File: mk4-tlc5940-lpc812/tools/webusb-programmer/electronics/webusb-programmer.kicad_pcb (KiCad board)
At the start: 2 copper layers, 38 x 20 mm, 29 parts, among them J1 USB_B_Micro, J2 Light Controller, Q1 PMV30UN, U1 MCP1703A-3302_SOT23, U2 SAMD21E15A-MU, U3 STMPS2141STR

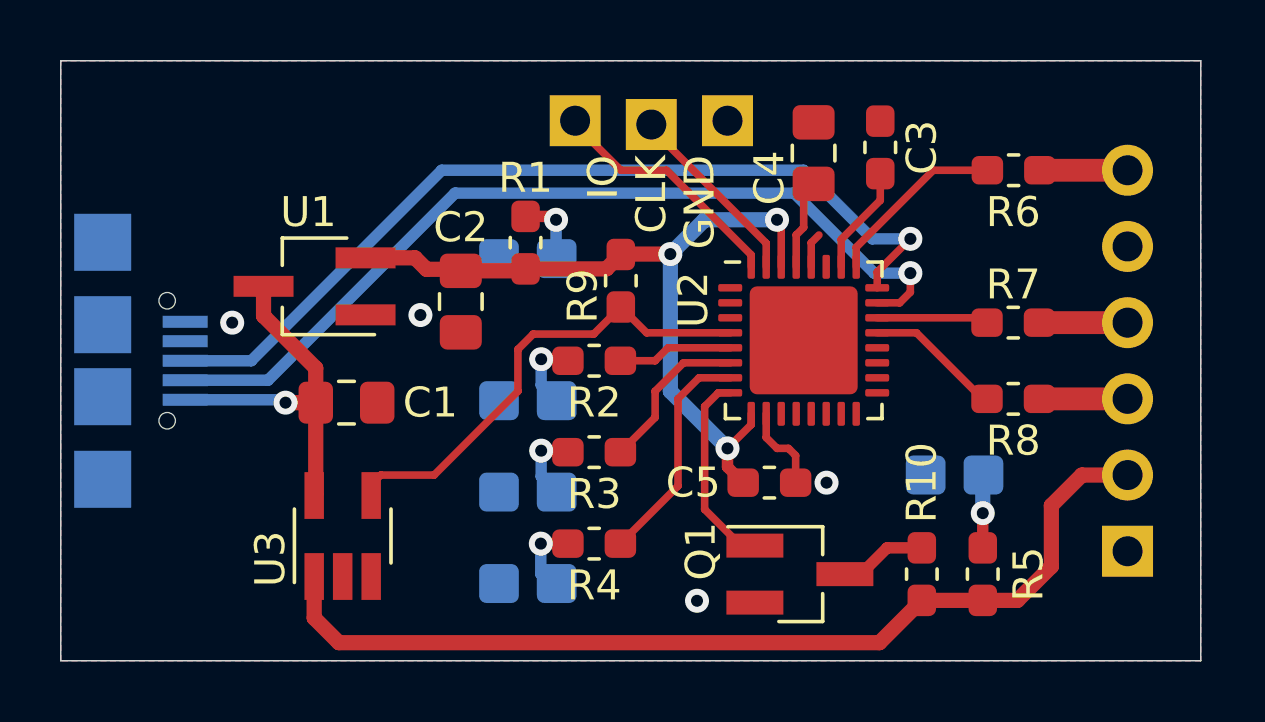
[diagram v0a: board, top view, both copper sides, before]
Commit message: Add CH3 IO and reannotate all components
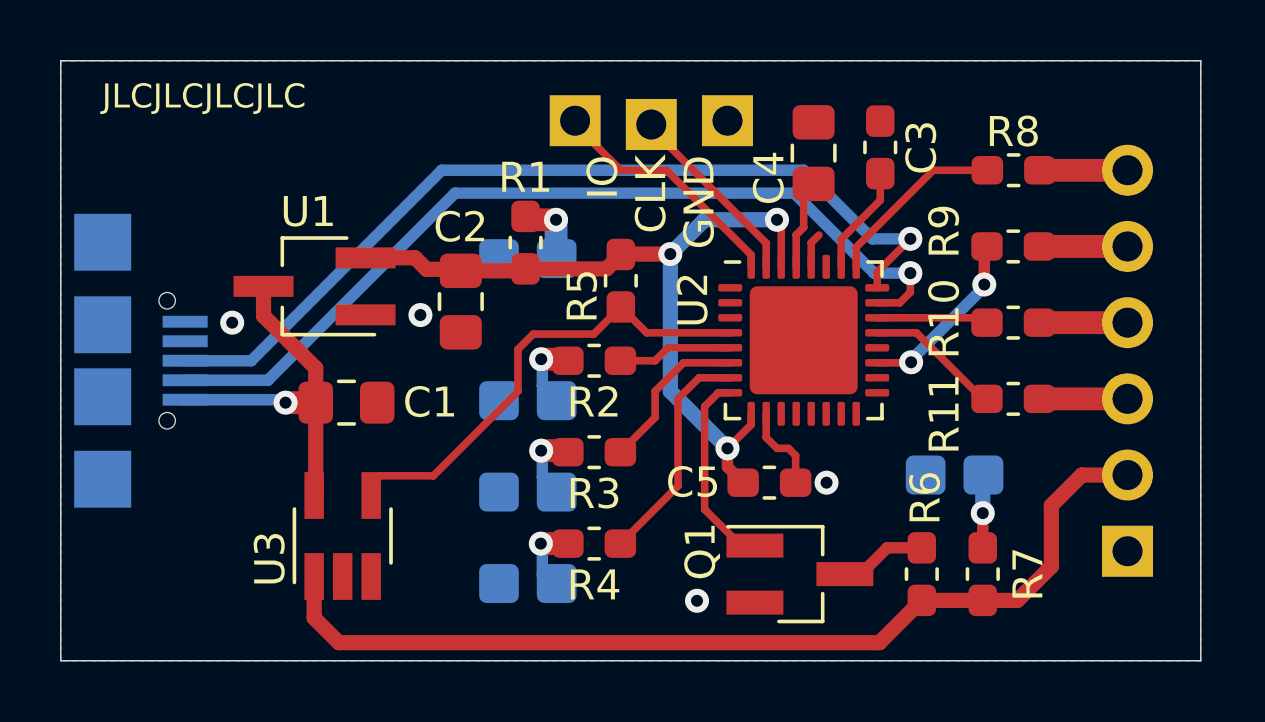
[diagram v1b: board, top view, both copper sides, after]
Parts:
- added R9: 1k, Resistor_SMD:R_0603_1608Metric_Pad1.05x0.95mm_HandSolder, F.Cu at (131.8, 96.2)
- renumbered R7 to R10, R8 to R11, R9 to R5, R10 to R6, R5 to R7, R6 to R8
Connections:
- U2 pad 19: Net-(U2-Pad19) -> /CH3
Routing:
- net /CH3: track 0.00 -> 6.05 mm, vias 0 -> 2
- net Net-(J2-Pad5): track 0.00 -> 2.94 mm
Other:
- board text added: "JLCJLCJLCJLC"

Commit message: Change LED resistor values after testing
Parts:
- R1, R7: value 1k2 -> 1k8
- R2: value 1k2 -> 2k7
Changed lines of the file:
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@@
       (effects (font (size 1 1) (thickness 0.15)))
     )
-    (fp_text value 1k2 (at 2.413 -0.127 90) (layer F.Fab)
+    (fp_text value 1k8 (at 2.413 -0.127 90) (layer F.Fab)
       (effects (font (size 1 1) (thickness 0.15)))
     )
@@
       (effects (font (size 1 1) (thickness 0.15)))
     )
-    (fp_text value 1k2 (at -2.413 0) (layer F.Fab)
+    (fp_text value 2k7 (at -2.413 0) (layer F.Fab)
       (effects (font (size 1 1) (thickness 0.15)))
     )
@@
       (effects (font (size 1 1) (thickness 0.15)))
     )
-    (fp_text value 1k2 (at 0.889 -1.143 90) (layer F.Fab)
-      (effects (font (size 1 1) (thickness 0.15)))
-    )
+    (fp_text value 1k8 (at 0.889 -1.143 90) (layer F.Fab)
+      (effects (font (size 1 1) (thickness 0.15)))
+    )

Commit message: Change bleed resistor to 10R
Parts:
- R6: value 100 -> 10
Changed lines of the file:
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@@
       (effects (font (size 1 1) (thickness 0.15)))
     )
-    (fp_text value 100 (at 2.54 -0.127 90) (layer F.Fab)
+    (fp_text value 10 (at 2.54 -0.127 90) (layer F.Fab)
       (effects (font (size 1 1) (thickness 0.15)))
     )

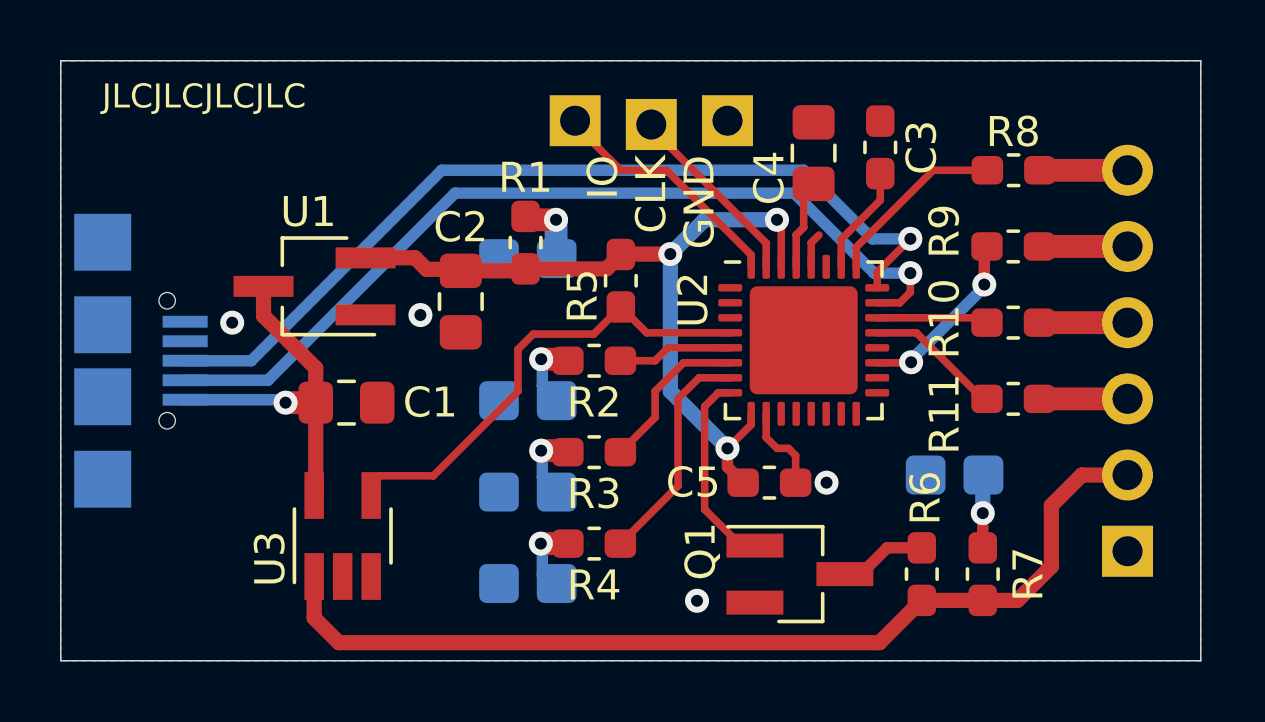
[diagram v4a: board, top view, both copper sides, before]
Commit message: Update WebUSB programmer layout
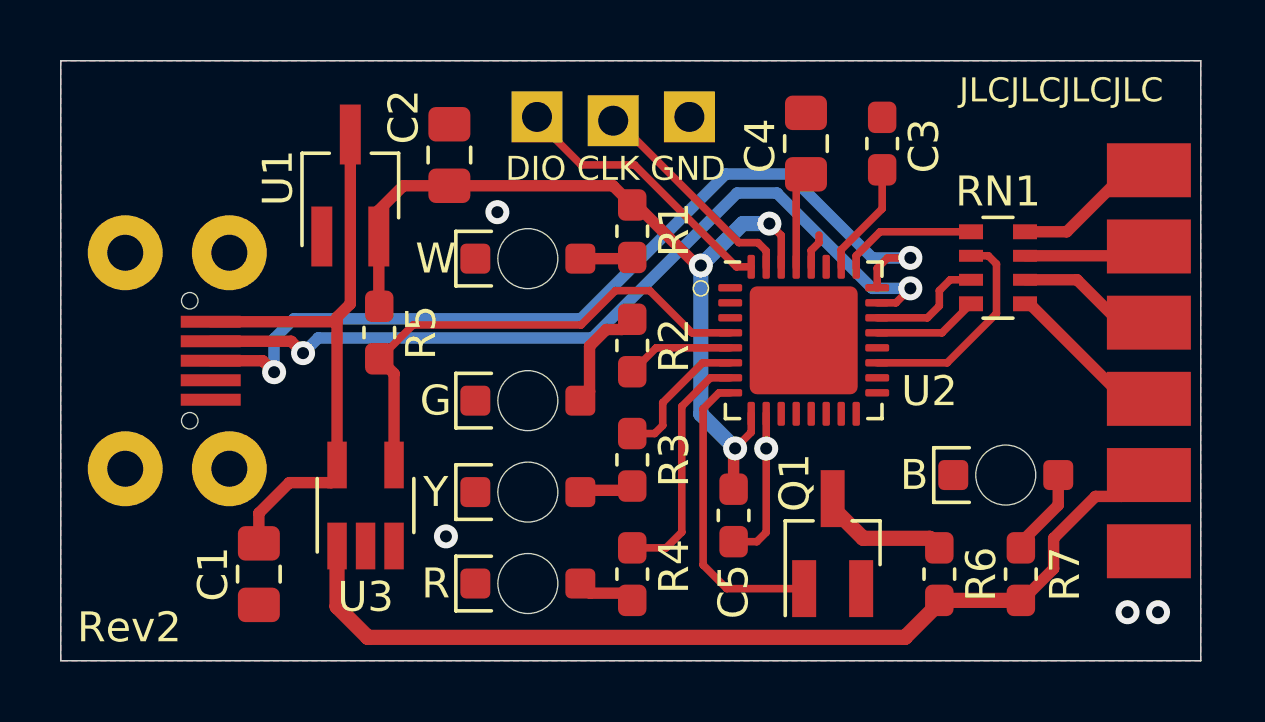
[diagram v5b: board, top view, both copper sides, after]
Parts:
- removed R10, R11, R8, R9: 1k, Resistor_SMD:R_0603_1608Metric_Pad1.05x0.95mm_HandSolder
- added RN1: 1k, Resistor_SMD:R_Array_Convex_4x0603, F.Cu at (131.2, 96.9)
- C2: value 47u/6V3 -> 10u
- D1: value MCU POWER -> White; footprint LED_SMD:LED_0805_2012Metric_Castellated -> WLA_LED_reverse_mount:LED_1204_reverse_mout; moved to F.Cu
- D2: value OK -> Green; footprint LED_SMD:LED_0805_2012Metric_Castellated -> WLA_LED_reverse_mount:LED_1204_reverse_mout; moved to F.Cu
- D3: value BUSY -> Yellow; footprint LED_SMD:LED_0805_2012Metric_Castellated -> WLA_LED_reverse_mount:LED_1204_reverse_mout; moved to F.Cu
- D4: value ERROR -> Red; footprint LED_SMD:LED_0805_2012Metric_Castellated -> WLA_LED_reverse_mount:LED_1204_reverse_mout; moved to F.Cu
- D5: value LC POWER -> Blue; footprint LED_SMD:LED_0805_2012Metric_Castellated -> WLA_LED_reverse_mount:LED_1204_reverse_mout; moved to F.Cu
- J1: footprint USB:Mirco_USB_Type_B_eBay_AliExpress -> USB:Mirco_USB_Type_B_LCSC_C40943; moved to F.Cu
- J2: footprint Connector_PinHeader_2.54mm:PinHeader_1x06_P2.54mm_Vertical -> WLA_pinheader:PinHeader_1x06_P2.54mm_Flat; moved to F.Cu
- moved R5 8.24 mm to (110.6, 99.1)
- moved C1 6.42 mm to (106.6, 107.1), turned to 270 degrees
- moved C2 4.90 mm to (113.0, 93.1), turned to 90 degrees
- moved R1 3.58 mm to (119.0, 95.7), turned to 270 degrees
- moved U1 3.57 mm to (109.7, 94.2), turned to 90 degrees
- moved D5 1.71 mm to (131.5, 103.8)
- moved R4 1.63 mm to (119.0, 107.1), turned to 270 degrees
- moved C5 1.62 mm to (122.4, 105.2), turned to 270 degrees
- moved Q1 1.49 mm to (125.7, 106.1), turned to 90 degrees
- moved J1 1.40 mm to (100.0, 100.0), turned to 270 degrees
- moved R2 1.37 mm to (119.0, 99.5), turned to 90 degrees
- moved R3 1.30 mm to (119.0, 103.3), turned to 270 degrees
- moved TP2 1.28 mm to (118.4, 92.0)
- moved TP1 1.28 mm to (115.9, 91.9)
- moved TP3 1.28 mm to (121.0, 91.9)
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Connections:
- J1 pad 4: Net-(J1-Pad4) -> (no net)
- U2 pad 1: Net-(U2-Pad1) -> (no net)
- U2 pad 11: Net-(U2-Pad11) -> (no net)
- U2 pad 12: Net-(U2-Pad12) -> (no net)
- U2 pad 13: Net-(U2-Pad13) -> (no net)
- U2 pad 14: Net-(U2-Pad14) -> (no net)
- U2 pad 15: Net-(U2-Pad15) -> (no net)
- U2 pad 16: Net-(U2-Pad16) -> (no net)
- U2 pad 17: Net-(U2-Pad17) -> (no net)
- U2 pad 18: Net-(U2-Pad18) -> (no net)
- U2 pad 2: Net-(U2-Pad2) -> (no net)
- U2 pad 20: Net-(U2-Pad20) -> (no net)
- U2 pad 27: Net-(U2-Pad27) -> (no net)
- U2 pad 3: Net-(U2-Pad3) -> (no net)
- U3 pad 3: Net-(U3-Pad3) -> (no net)
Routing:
- net +5V: track 12.2 -> 19.9 mm, vias 1 -> 0
- net /SHORT: track 6.65 -> 10.0 mm
- net +3V3: track 26.3 -> 29.2 mm
- net Net-(J2-Pad3): track 2.78 -> 5.62 mm
- net Net-(J2-Pad6): track 2.77 -> 4.78 mm
- net GND: track 4.35 -> 6.33 mm, vias 4 -> 5
- net Net-(J2-Pad4): track 2.78 -> 4.52 mm
- net Net-(Q1-Pad3): track 2.93 -> 4.41 mm
- net /USB-DM: track 29.8 -> 28.3 mm, vias 1 -> 2
- net /ISP: track 5.94 -> 4.53 mm
- net /SWCLK: track 6.33 -> 7.74 mm
- net Net-(D2-Pad2): track 2.51 -> 3.74 mm, vias 1 -> 0
- net /CH3: track 6.05 -> 7.27 mm, vias 2 -> 0
- net Net-(J2-Pad5): track 2.94 -> 4.05 mm
- net /EN: track 16.0 -> 17.0 mm
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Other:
- board text added: "B"
- board text added: "DIO CLK GND"
- board text added: "G"
- board text added: "R"
- board text added: "Rev2"
- board text added: "W"
- board text added: "Y"
- board text removed: "IO CLK GND"

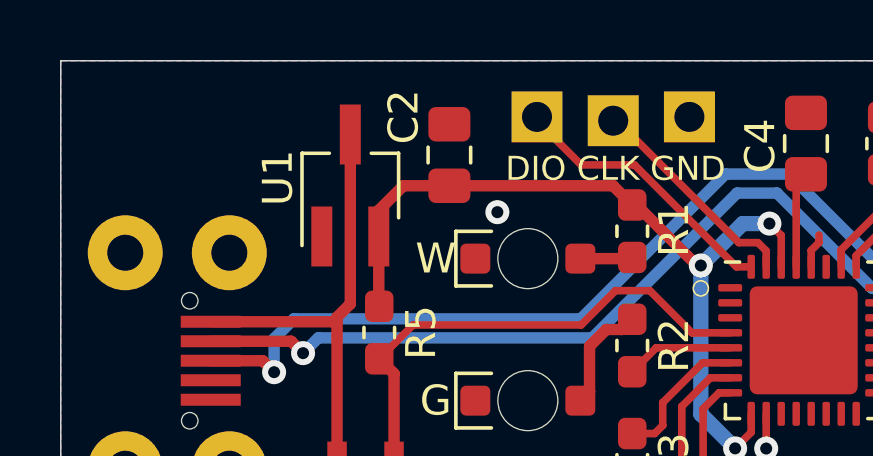
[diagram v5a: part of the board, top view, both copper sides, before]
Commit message: Replace expensive 47u cap with MLCC 10u 0603
Tested on a prototype and working without issue
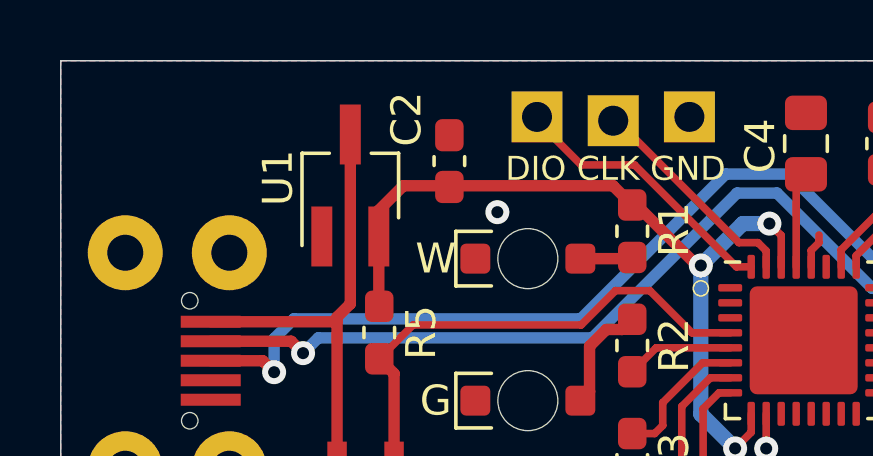
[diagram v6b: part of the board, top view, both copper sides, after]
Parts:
- C2: footprint Capacitor_SMD:C_0805_2012Metric_Pad1.15x1.40mm_HandSolder -> Capacitor_SMD:C_0603_1608Metric_Pad1.08x0.95mm_HandSolder
- D1: value White -> MCU POWER
- D2: value Green -> OK
- D3: value Yellow -> BUSY
- D4: value Red -> ERROR
- D5: value Blue -> LC POWER
- moved C2 0.20 mm to (113.0, 93.3)

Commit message: Tweak the layout
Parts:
- moved C4 0.76 mm to (125.6, 92.8)
- moved C3 0.51 mm to (127.9, 92.8)
- moved TP1 0.19 mm to (116.1, 91.9)
- moved TP2 0.19 mm to (118.6, 92.0)
- moved TP3 0.19 mm to (121.1, 91.9)
- turned R1 to 90 degrees
- turned R2 to 270 degrees
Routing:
- net GND: track 6.33 -> 2.32 mm, vias 5 -> 4
- net +3V3: track 29.2 -> 31.4 mm
- net Net-(D2-Pad2): track 3.74 -> 2.13 mm
- net Net-(D1-Pad2): track 1.75 -> 2.66 mm
- net /RESET: track 3.80 -> 4.31 mm
